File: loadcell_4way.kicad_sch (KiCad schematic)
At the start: 99 parts, among them J1 USB_B_Micro, J2 Battery, J3 OLDED_Screen, J4 T4145015051-001, J5 T4145015051-001, J6 T4145015051-001, J7 T4145015051-001, Q1 FDS6892A, Q2 BSS138, Q3 SM2331PSA P-MOSFET, Q4 S8550, Q5 BSS138, SW1 SW_Push, SW2 SW_Push, SW3 SW_Push, U1 FS312F-G, U2 MT3608, U3 TP4056, U4 CH330N, U5 LM1117-3.3, U6 ESP-12E, U7 HX711

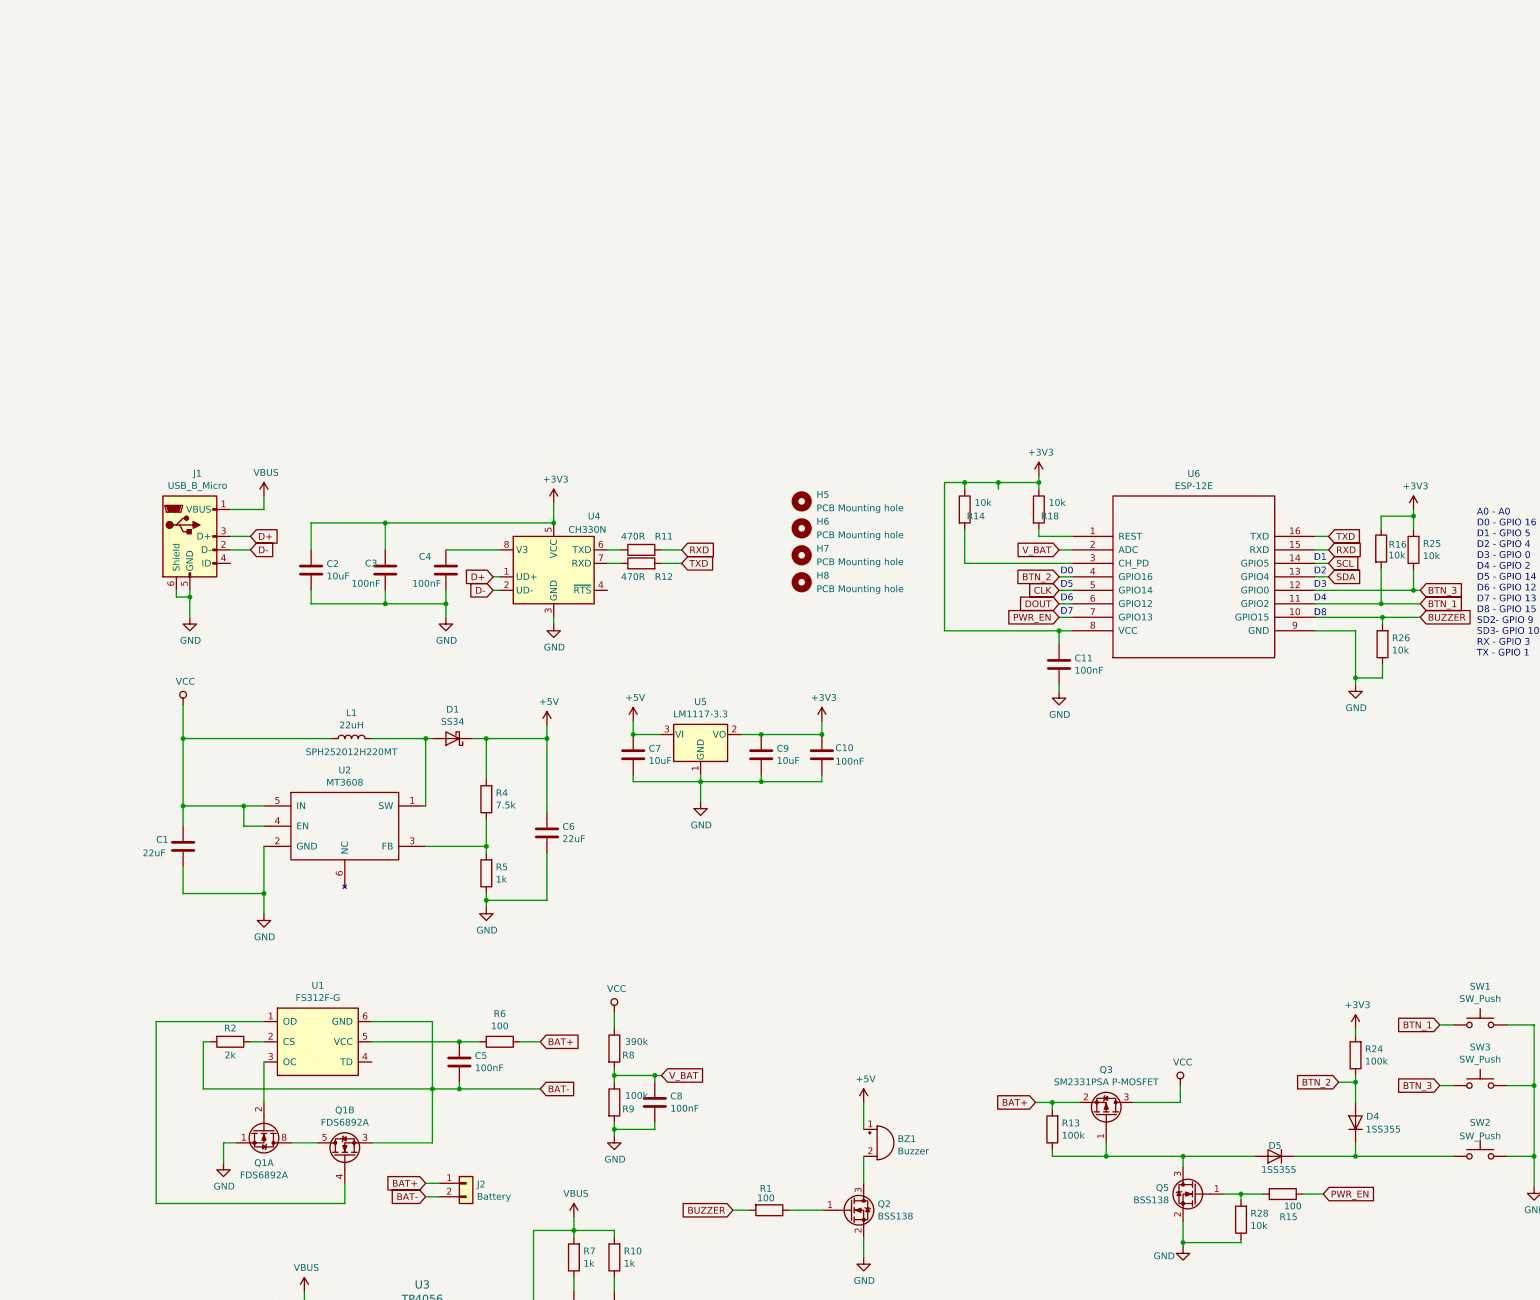
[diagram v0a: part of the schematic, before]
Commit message: esp32-c3 ch340c
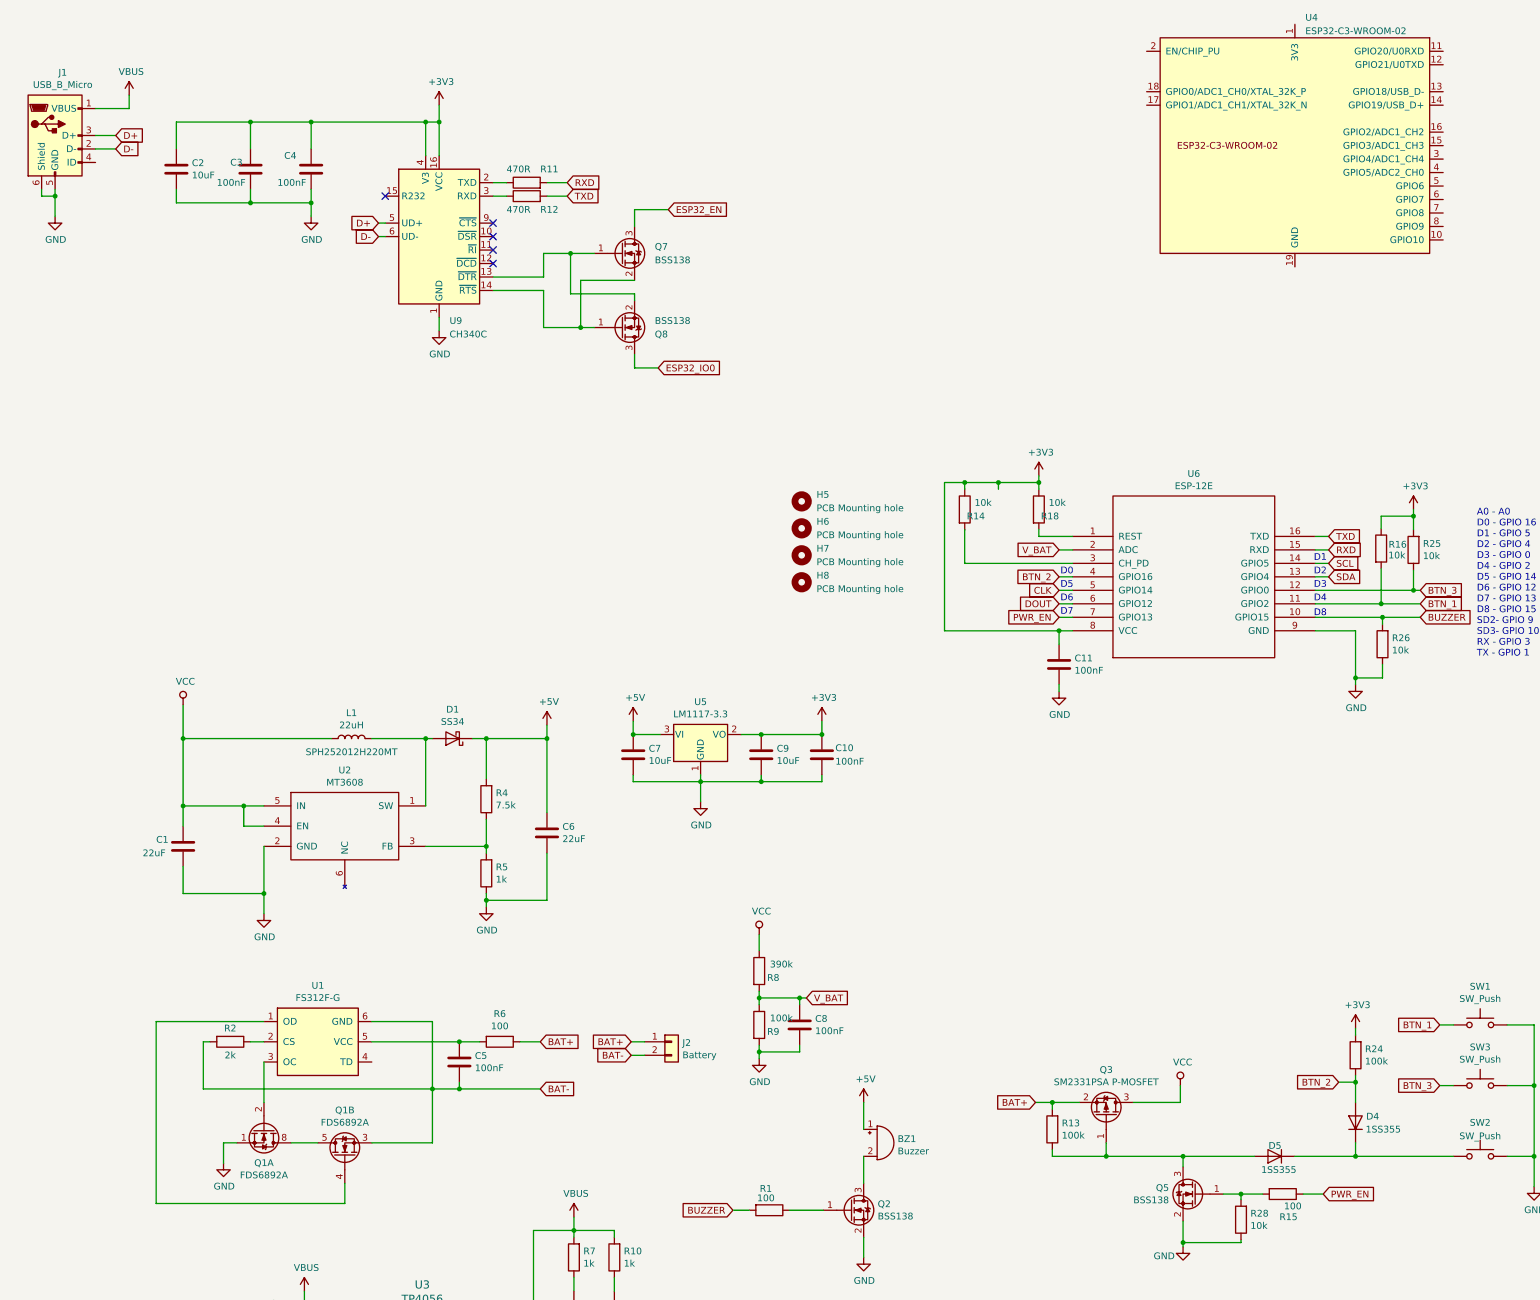
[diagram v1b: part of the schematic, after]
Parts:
- removed U4: CH330N, Package_SO:SOIC-8_3.9x4.9mm_P1.27mm, symbol Interface_USB:CH330N
- added Q7, Q8: BSS138, Package_TO_SOT_SMD:SOT-23, symbol Transistor_FET:BSS138
- added U4: ESP32-C3-WROOM-02, Espressif:ESP32-C3-WROOM-02, symbol esp:ESP32-C3-WROOM-02
- added U9: CH340C, Package_SO:SOIC-16_3.9x9.9mm_P1.27mm, symbol Interface_USB:CH340C
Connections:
- net +3V3: now also C4.1, U9.16 (VCC), U9.4 (V3)
- net D+: now also U9.5 (UD+)
- net D-: now also U9.6 (UD-)
- net GND: now also U9.1 (GND)
- net at R11.1: now also U9.2 (TXD)
- net at R12.1: now also U9.3 (RXD)
- new net: Q7.1 (G), Q8.2 (S), U9.13 (~{DTR})
- new net: Q7.2 (S), Q8.1 (G), U9.14 (~{RTS})
- new net: U4.19 (GND), U4.9 (GND)
- new net ESP32_EN: Q7.3 (D)
- new net ESP32_IO0: Q8.3 (D)
- no-connect marks 0 -> 5
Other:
- moved on the sheet: C8, J2, R8, R9

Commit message: wip
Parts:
- removed C11, C13 (x2), C14 (x4), C16 (x2): 100nF, Capacitor_SMD:C_0603_1608Metric, symbol Device:C
- removed C12 (x2), C15 (x2): 10uF, Capacitor_SMD:C_0603_1608Metric, symbol Device:C
- removed Q4 (x2): S8550, Package_TO_SOT_SMD:SOT-23, symbol Device:Q_PNP_BEC
- removed R14, R16, R18, R25, R26: 10k, Resistor_SMD:R_0603_1608Metric, symbol Device:R
- removed R19 (x2), R27 (x2): 0R, Resistor_SMD:R_0603_1608Metric, symbol Device:R
- removed R20 (x2): 20k, Resistor_SMD:R_0603_1608Metric, symbol Device:R
- removed R21 (x2): 8k2, Resistor_SMD:R_0603_1608Metric, symbol Device:R
- removed R22 (x4), R23 (x4): 1k, Resistor_SMD:R_0603_1608Metric, symbol Device:R
- removed U6: ESP-12E, ESP8266:ESP-12, symbol ESP8266:ESP-12E
- removed U7 (x2): HX711, Package_SO:SOP-16_4.55x10.3mm_P1.27mm, symbol ForceGaugeSymbols:HX711
- added C10, C14 (x4), C16 (x8), C4, C8: 100nF, Capacitor_SMD:C_0603_1608Metric, symbol Device:C
- added C2, C7, C9: 10uF, Capacitor_SMD:C_0603_1608Metric, symbol Device:C
- added R11 (x2), R16 (x2), R23, R25: 10k, Resistor_SMD:R_0603_1608Metric, symbol Device:R
- added R22 (x4), R23 (x4): 1k, Resistor_SMD:R_0603_1608Metric, symbol Device:R
- added R23: 0R, Resistor_SMD:R_0603_1608Metric, symbol Device:R
- added R25 (x2): 4k7, Resistor_SMD:R_0603_1608Metric, symbol Device:R
- added R8: 390k, Resistor_SMD:R_0603_1608Metric, symbol Device:R
- added R9: 100k, Resistor_SMD:R_0603_1608Metric, symbol Device:R
- added U10: ADS1234IPW, Loadcell:SOP65P640X120-28N, symbol ads1234:ADS1234IPW
- added U5: LM1117-3.3, Package_TO_SOT_SMD:SOT-223, symbol Regulator_Linear:LM1117-3.3
- H1, H2, H3, H4: footprint forcegauge:MountingHole_2mm_OLED -> Loadcell:MountingHole_2mm_OLED
- H5, H6, H7, H8: footprint forcegauge:MountingHole_2mm_OLED -> MountingHole:MountingHole_3.2mm_M3
- U3: footprint forcegauge:SOP8-PP -> Loadcell:SOP8-PP
- U4: footprint Espressif:ESP32-C3-WROOM-02 -> Loadcell:ESP32-C3-WROOM-02
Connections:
- net E2+ is gone; now on net +3.3VA: J6.1, J7.1
- net ESP32_IO0 is gone; now on net ESP32_IO9: Q8.3 (D)
- net SCL is gone; now on net ESP32_IO9: J3.3 (Pin_3)
- net V_BAT is gone; now on net VBAT_FB: C8.1, R8.2, R9.1
- net +3V3: now also U4.1 (3V3), C16.1, C4.1, R16.1, R16.1, R23.1, R25.2, R25.2, R25.2, U10.1 (DVDD), U10.23 (GAIN0), U10.24 (GAIN1), U10.25 (SPEED)
- net +5V: now also C7.1, U5.3 (VI)
- net A1+: now also C14.1, R22.2, U10.11 (AINP1); no longer J4.4
- net A1-: now also C14.2, R23.2, U10.12 (AINN1); no longer J4.3
- net A2+: now also C14.1, R22.2, U10.18 (AINP2); no longer J6.4
- net A2-: now also C14.2, R23.2, U10.17 (AINN2); no longer J6.3
- net BTN_1: now also U4.15 (GPIO3/ADC1_CH3), R16.2
- net BTN_2: now also U4.13 (GPIO18/USB_D-)
- net BTN_3: now also U4.16 (GPIO2/ADC1_CH2), R25.1
- net BUZZER: now also U4.10 (GPIO10)
- net CLK: now also U4.5 (GPIO6), U10.27 (SCLK)
- net DOUT: now also U4.6 (GPIO7), U10.28 (~{DRDY~{/DOUT})
- net ESP32_EN: now also U4.2 (EN/CHIP_PU), C2.1, R16.2
- net GND: now also U4.19 (GND), U4.9 (GND), C16.2, C2.2, C4.2, C8.2, R23.2, R9.2, U10.2 (DGND), U10.3 (CLKIN/XTAL1), U10.5 (DGND), U10.6 (DGND)
- net PWR_EN: now also U4.14 (GPIO19/USB_D+)
- net RXD: now also U4.11 (GPIO20/U0RXD)
- net SDA: now also U4.7 (GPIO8), R25.1
- net TXD: now also U4.12 (GPIO21/U0TXD)
- net VBUS: now also R8.1
- net at Q8.2 (S), U9.13 (~{DTR}): now also R11.1; no longer Q7.1 (G)
- net at Q7.2 (S), U9.14 (~{RTS}): now also R11.1; no longer Q8.1 (G)
- net VBUS_FB: now reaches U4.17 (GPIO1/ADC1_CH1/XTAL_32K_N)
- net VBUS_FB: now also C8.1, R8.2, R9.1
- net VBAT_FB: now reaches U4.18 (GPIO0/ADC1_CH0/XTAL_32K_P)
- net MUX0: now reaches U4.3 (GPIO4/ADC1_CH4)
- net MUX0: now also U10.8 (A0)
- net MUX1: now reaches U4.4 (GPIO5/ADC2_CH0)
- net MUX1: now also U10.7 (A1)
- net ESP32_IO9: now reaches U4.8 (GPIO9)
- net ESP32_IO9: now also R25.1
- net B1+: no longer names the net of J5.4
- net B1+: now also R23.1
- net B1-: no longer names the net of J5.3
- net B1-: now also R22.1
- net B2+: no longer names the net of J7.4
- net B2+: now also R23.1
- net B2-: no longer names the net of J7.3
- net B2-: now also R22.1
- net E1+ renamed +3.3VA
- net +3.3VA: now also C10.1, C16.1, C16.1, C16.1, C16.1, C16.1, C16.1, C9.1, U10.20 (REFP), U10.22 (AVDD), U5.2 (VO)
- net E1-: no longer names the net of J5.2
- net E1-: now also C16.2; no longer J4.2
- net E2-: no longer names the net of J7.2
- net E2-: now also C16.2; no longer J6.2
- new net: J4.3, R22.1
- new net: C16.2, U10.10 (CAP_2)
- new net: R23.2, U10.26 (~{PDWN})
- new net: C16.1, U10.9 (CAP_1)
- new net: J4.4, R23.1
- new net: Q8.1 (G), R11.2
- new net: Q7.1 (G), R11.2
- new net: C16.2, J6.2
- new net: J6.3, R22.1
- new net: C16.2, J4.2
- new net: J6.4, R23.1
- new net A3+: C14.1, R22.2, U10.13 (AINP3)
- new net A3-: C14.2, R23.2, U10.14 (AINN3)
- new net A4+: C14.1, R22.2, U10.16 (AINP4)
- new net A4-: C14.2, R23.2, U10.15 (AINN4)
- new net GNDA: C10.2, C16.2, C16.2, C7.2, C9.2, R23.1, U10.19 (REFN), U10.21 (AGND), U5.1 (GND)
- no-connect marks 5 -> 6
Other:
- note removed: "A0 - A0 D0 - GPIO 16 D1 - GPIO 5 D2 - GPIO 4 D3 - GPIO 0 D4 - GPIO 2 D5 - GPIO 14 D6 - GPIO 12 D7 - GPIO 13 D8 - GPIO 15 SD2- GPIO 9 SD3- GPIO 10 RX - GPIO 3 TX - GPIO 1"
- note removed: "D0"
- note removed: "D1"
- note removed: "D2"
- note removed: "D3"
- note removed: "D4"
- note removed: "D5"
- note removed: "D6"
- note removed: "D7"
- note removed: "D8"
- moved on the sheet: C1, C10, C2, C3, C4, C6, C7, C8, C9, D1, D3, J1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

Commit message: wip
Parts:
- removed J4, J5, J6, J7: T4145015051-001, TE_T4145015051-001, symbol Loadcell:T4145015051-001
- removed U5: LM1117-3.3, Package_TO_SOT_SMD:SOT-223, symbol Regulator_Linear:LM1117-3.3
- added J10, J4, J5, J6: Conn_01x05, Connector_Phoenix_MSTB:PhoenixContact_MSTBA_2,5_5-G-5,08_1x05_P5.08mm_Horizontal, symbol Connector_Generic:Conn_01x05
- added R4: 2k2, Resistor_SMD:R_0603_1608Metric, symbol Device:R
- added R4: 10k, Resistor_SMD:R_0603_1608Metric, symbol Device:R
- added U7: AP2127K-ADJ, Package_TO_SOT_SMD:SOT-23-5, symbol Regulator_Linear:AP2127K-ADJ
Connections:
- net +3.3VA: now also J10.1 (Pin_1), J4.1 (Pin_1), J5.1 (Pin_1), J6.1 (Pin_1), R4.2, U7.5 (VOUT)
- net +5V: now also U7.1 (VIN), U7.3 (EN)
- net GND: now also J10.5 (Pin_5), J4.5 (Pin_5), J5.5 (Pin_5), J6.5 (Pin_5)
- net GNDA: now also R4.1, U7.2 (GND)
- net at R23.1: now also J4.4 (Pin_4)
- net at C16.2: now also J4.2 (Pin_2)
- net at R22.1: now also J4.3 (Pin_3)
- net at R22.1: now also J10.3 (Pin_3)
- net at C16.2: now also J6.2 (Pin_2)
- net at R23.1: now also J10.4 (Pin_4)
- net at R22.1: now also J6.3 (Pin_3)
- net at R23.1: now also J6.4 (Pin_4)
- net at C16.2: now also J5.2 (Pin_2)
- net at R22.1: now also J5.3 (Pin_3)
- net at C16.2: now also J10.2 (Pin_2)
- net at R23.1: now also J5.4 (Pin_4)
- new net: R4.1, R4.2, U7.4 (ADJ)
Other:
- moved on the sheet: C10, C2, C4, C7, C9, H5, H6, H7, H8, R16, R25, U4

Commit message: wip
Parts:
- added C10 (x2), C14 (x8): 100nF, Capacitor_SMD:C_0603_1608Metric, symbol Device:C
- added FB1: FerriteBead, symbol Device:FerriteBead
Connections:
- net +3.3VA: no longer C10.1, C16.1, C16.1, C16.1, C16.1, C16.1, C9.1, J10.1 (Pin_1), J4.1 (Pin_1), J5.1 (Pin_1), J6.1 (Pin_1), R4.2, U10.22 (AVDD), U7.5 (VOUT)
- net +5V: now also C10.1, FB1.1; no longer C7.1, U7.1 (VIN), U7.3 (EN)
- net A1+: now also C14.1
- net A1-: now also C14.1
- net A2+: now also C14.1
- net A2-: now also C14.1
- net A3+: now also C14.1
- net A3-: now also C14.1
- net A4+: now also C14.1
- net A4-: now also C14.1
- net GNDA: now also C10.2, C10.2, C14.2, C14.2, C14.2, C14.2, C14.2, C14.2, C14.2, C14.2
- new net: C10.1, C7.1, FB1.2, U7.1 (VIN), U7.3 (EN)
- new net VDDA: C10.1, C16.1, C16.1, C16.1, C16.1, C16.1, C9.1, J10.1 (Pin_1), J4.1 (Pin_1), J5.1 (Pin_1), J6.1 (Pin_1), R4.2, U10.22 (AVDD), U7.5 (VOUT)
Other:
- moved on the sheet: C10, C7, C9, R4, U7

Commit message: wip
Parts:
- FB1: footprint (none) -> Inductor_SMD:L_1206_3216Metric
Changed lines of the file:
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@@
       (effects (font (size 1.27 1.27)))
     )
-    (property "Footprint" "" (at 299.72 248.158 90)
+    (property "Footprint" "Inductor_SMD:L_1206_3216Metric" (at 299.72 248.158 90)
       (effects (font (size 1.27 1.27)) hide)
     )

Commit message: PCB wip
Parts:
- added C16: 100nF, Capacitor_SMD:C_0603_1608Metric, symbol Device:C
- added R23 (x2): 0R, Resistor_SMD:R_0603_1608Metric, symbol Device:R
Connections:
- net +3.3VA is gone; now on net VDDA: C16.1, U10.20 (REFP)
- net A2+: now also U10.13 (AINP3); no longer U10.18 (AINP2)
- net A2-: now also U10.14 (AINN3); no longer U10.17 (AINN2)
- net A3+: now also U10.16 (AINP4); no longer U10.13 (AINP3)
- net A3-: now also U10.15 (AINN4); no longer U10.14 (AINN3)
- net A4+: now also U10.18 (AINP2); no longer U10.16 (AINP4)
- net A4-: now also U10.17 (AINN2); no longer U10.15 (AINN4)
- net GND: now also R23.1; no longer J10.5 (Pin_5), J4.5 (Pin_5), J5.5 (Pin_5), J6.5 (Pin_5)
- net GNDA: now also C16.2, C16.2, C16.2, C16.2, J10.2 (Pin_2), J4.2 (Pin_2), J5.2 (Pin_2), J6.2 (Pin_2), C16.2, R23.1
- net VDDA: now also C16.1
- new net Earth: J10.5 (Pin_5), J4.5 (Pin_5), J5.5 (Pin_5), J6.5 (Pin_5), R23.2, R23.2
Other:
- note added: "Routing is better when these are swapped"
- moved on the sheet: C16

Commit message: pcb wip
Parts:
- removed J10, J4, J5, J6: Conn_01x05, Connector_Phoenix_MSTB:PhoenixContact_MSTBA_2,5_5-G-5,08_1x05_P5.08mm_Horizontal, symbol Connector_Generic:Conn_01x05
- added J4, J5, J6, J7: T4145015051-001, TE_T4145015051-001, symbol Loadcell:T4145015051-001
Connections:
- net GNDA: now also J4.2, J5.2, J6.2, J7.2
- net VDDA: now also J4.1, J5.1, J6.1, J7.1
- net at R23.1: now also J5.4
- net at R22.1: now also J4.3
- net at R22.1: now also J5.3
- net at R23.1: now also J4.4
- net at R22.1: now also J6.3
- net at R23.1: now also J6.4
- net at R22.1: now also J7.3
- net at R23.1: now also J7.4
- net Earth renamed SHIELD
- net SHIELD: now also J4.5, J5.5, J6.5, J7.5

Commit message: pcb wip
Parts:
- removed C14 (x9), C16 (x3): 100nF, Capacitor_SMD:C_0603_1608Metric, symbol Device:C
- removed R22 (x3), R23 (x3): 1k, Resistor_SMD:R_0603_1608Metric, symbol Device:R
- added C14 (x9), C16 (x3): 100nF, Capacitor_SMD:C_0603_1608Metric, symbol Device:C
- added R22 (x3), R23 (x3): 1k, Resistor_SMD:R_0603_1608Metric, symbol Device:R
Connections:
- net A2+: now also C14.1, C14.1, R22.2
- net A2-: now also C14.1, C14.2, R23.2
- net A3+: now also C14.1, C14.1, R22.2
- net A3-: now also C14.1, C14.2, R23.2
- net A4+: now also C14.1, C14.1, R22.2
- net A4-: now also C14.1, C14.2, R23.2
- net GNDA: now also J4.3, J5.3, J6.3, J7.3, C14.2, C14.2, C14.2, C14.2, C14.2, C14.2, C16.2, C16.2, C16.2; no longer J4.2, J5.2, J6.2, J7.2
- net VDDA: now also C16.1, C16.1, C16.1
- net at J5.4: now also R22.1
- net at J6.4: now also R22.1
- net at R22.1: now also J4.4; no longer J4.3
- net at R23.1: now also J4.2; no longer J4.4
- net at J7.4: now also R22.1
- new net: J6.2, R23.1
- new net: J7.2, R23.1
- new net: J5.2, R23.1
